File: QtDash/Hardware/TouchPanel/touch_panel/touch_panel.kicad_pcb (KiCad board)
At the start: 2 copper layers, 11 parts, among them U1 74LVC2G14, U2 74LVC2G14, U3 AT42QT1070-S

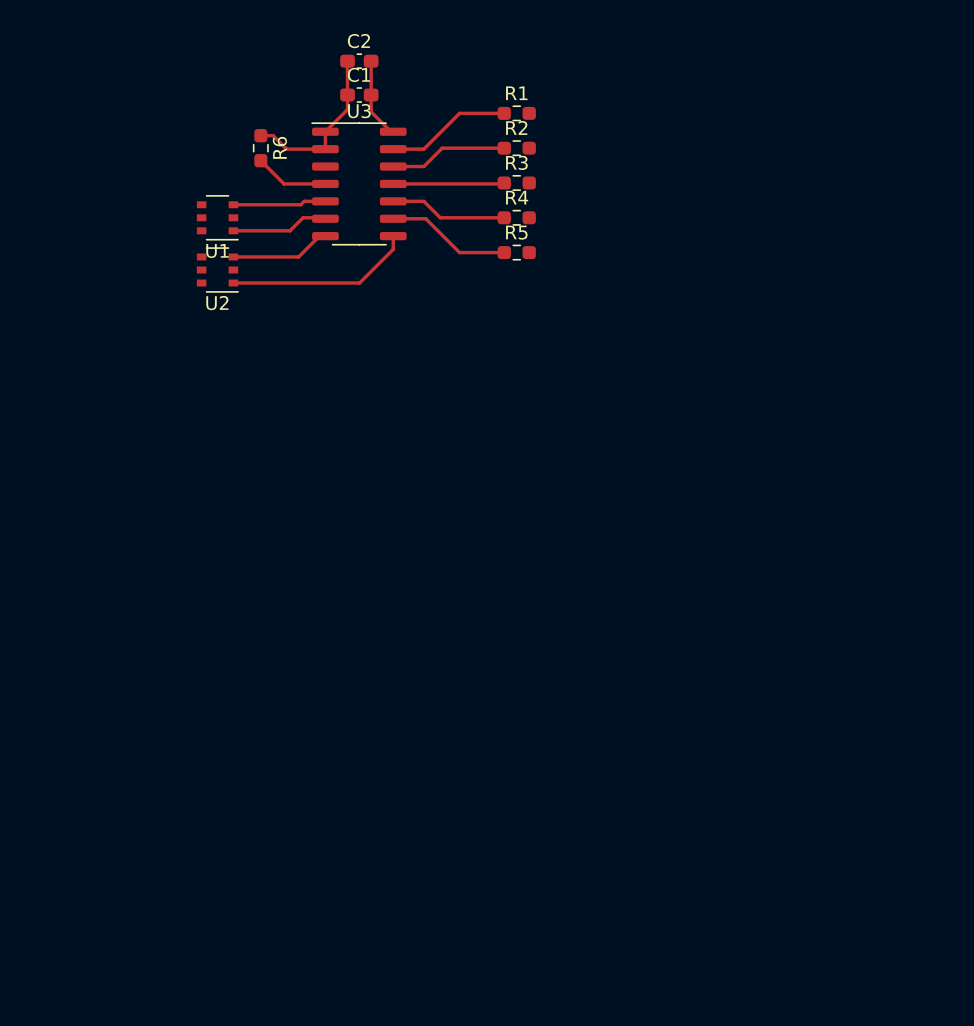
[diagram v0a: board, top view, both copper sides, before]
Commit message: bugfix/hardware-revc-fixes: 	- first draft of layout for control button board 	- added symbol + footprint for capacitive touch button 12.5mm square
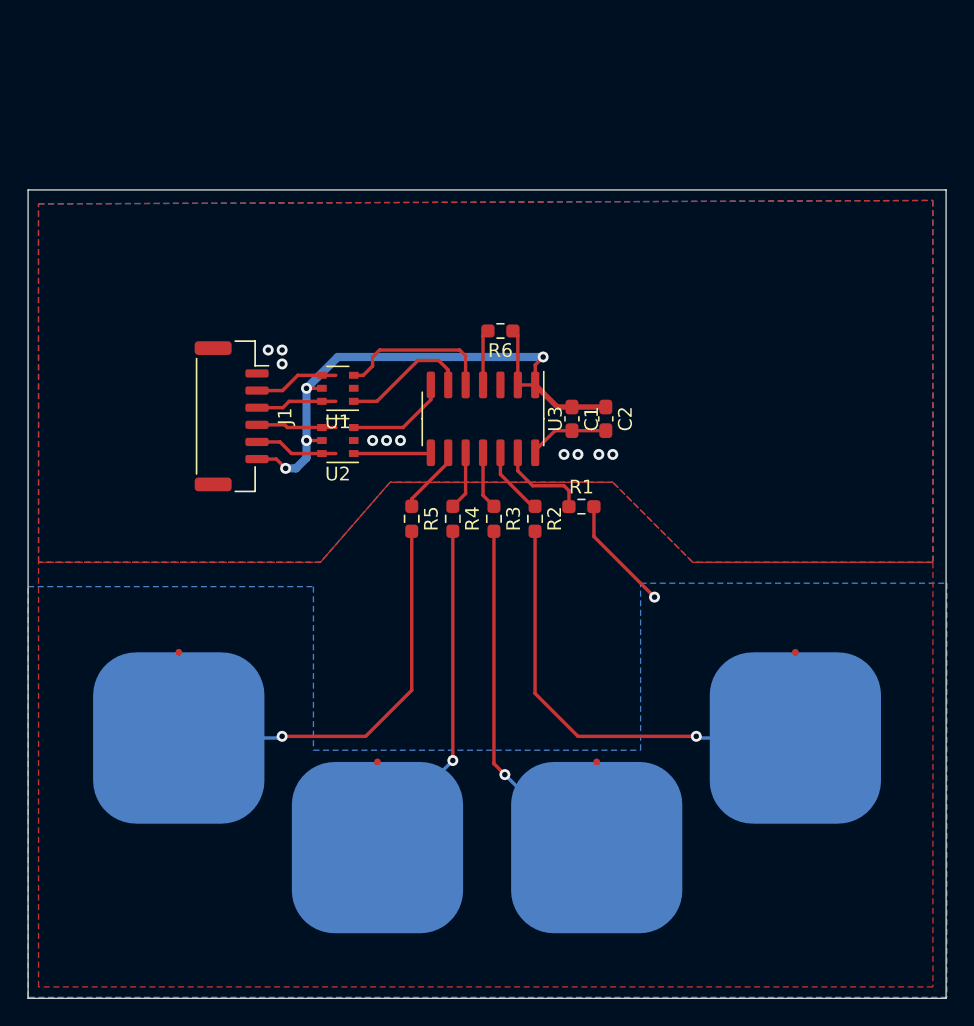
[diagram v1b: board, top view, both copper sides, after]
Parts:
- added J1: Conn_01x06_Male, Connector_JST:JST_GH_SM06B-GHS-TB_1x06-1MP_P1.25mm_Horizontal, F.Cu at (130.7, 92.0)
- added SW1: CapTouch_pad, volvodash:CAPTOUCH_12.5, B.Cu at (171.8, 115.4)
- added SW2: CapTouch_pad, volvodash:CAPTOUCH_12.5, B.Cu at (157.3, 123.4)
- added SW3: CapTouch_pad, volvodash:CAPTOUCH_12.5, B.Cu at (141.3, 123.4)
- added SW4: CapTouch_pad, volvodash:CAPTOUCH_12.5, B.Cu at (126.8, 115.4)
- moved C2 31.7 mm to (158.0, 92.1), turned to -90 degrees
- moved R1 29.1 mm to (156.2, 98.6)
- moved C1 28.3 mm to (155.5, 92.1), turned to -90 degrees
- moved R2 27.1 mm to (152.8, 99.4), turned to -90 degrees
- moved R3 24.6 mm to (149.8, 99.4), turned to -90 degrees
- moved R4 22.5 mm to (146.8, 99.4), turned to -90 degrees
- moved R6 22.0 mm to (150.3, 85.7), turned to 180 degrees
- moved R5 20.9 mm to (143.8, 99.4), turned to -90 degrees
- moved U3 19.4 mm to (149.0, 92.1), turned to -90 degrees
- moved U1 15.2 mm to (138.4, 89.9)
- moved U2 15.2 mm to (138.4, 93.7)
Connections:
- R1 pad 2: unconnected-(R1-Pad2) -> /GUARD_LOOP
- R2 pad 2: unconnected-(R2-Pad2) -> Net-(R2-Pad2)
- R3 pad 2: unconnected-(R3-Pad2) -> Net-(R3-Pad2)
- R4 pad 2: unconnected-(R4-Pad2) -> Net-(R4-Pad2)
- R5 pad 2: unconnected-(R5-Pad2) -> Net-(R5-Pad2)
- U1 pad 4: unconnected-(U1-Pad4) -> /USER_INPUT4
- U1 pad 6: unconnected-(U1-Pad6) -> /USER_INPUT3
- U2 pad 4: unconnected-(U2-Pad4) -> /USER_INPUT2
- U2 pad 6: unconnected-(U2-Pad6) -> /USER_INPUT1
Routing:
- net Net-(R3-Pad2): track 0.00 -> 35.5 mm, vias 0 -> 1
- net Net-(R2-Pad2): track 0.00 -> 34.2 mm, vias 0 -> 1
- net Net-(R4-Pad2): track 0.00 -> 33.9 mm, vias 0 -> 1
- net Net-(R5-Pad2): track 0.00 -> 32.0 mm, vias 0 -> 1
- net VCC: track 12.2 -> 43.2 mm, vias 0 -> 4
- net /GUARD_LOOP: track 0.00 -> 8.44 mm, vias 0 -> 1
- net /OUT1: track 13.6 -> 5.65 mm
- net /USER_INPUT4: track 0.00 -> 6.22 mm
- net /USER_INPUT1: track 0.00 -> 6.11 mm
- net /USER_INPUT3: track 0.00 -> 5.95 mm
- net /USER_INPUT2: track 0.00 -> 5.91 mm
- net /OUT4: track 6.82 -> 11.6 mm
- net /KEY3: track 8.60 -> 4.29 mm
- net /KEY4: track 9.12 -> 5.01 mm
- net /KEY2: track 8.13 -> 4.24 mm
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- added copper zone on B.Cu, net /GUARD_LOOP
- added copper zone on B.Cu, net GND
- added copper zone on F.Cu, net GND
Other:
- board outline added: 67 x 59 mm

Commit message: bugfix/hardware-revc-fixes: 	- finalized touch panel rev A 	- Rev A touch panel board sent to fab 	- added stl files for small guage slot cover (whole and cutout for touch panel board)
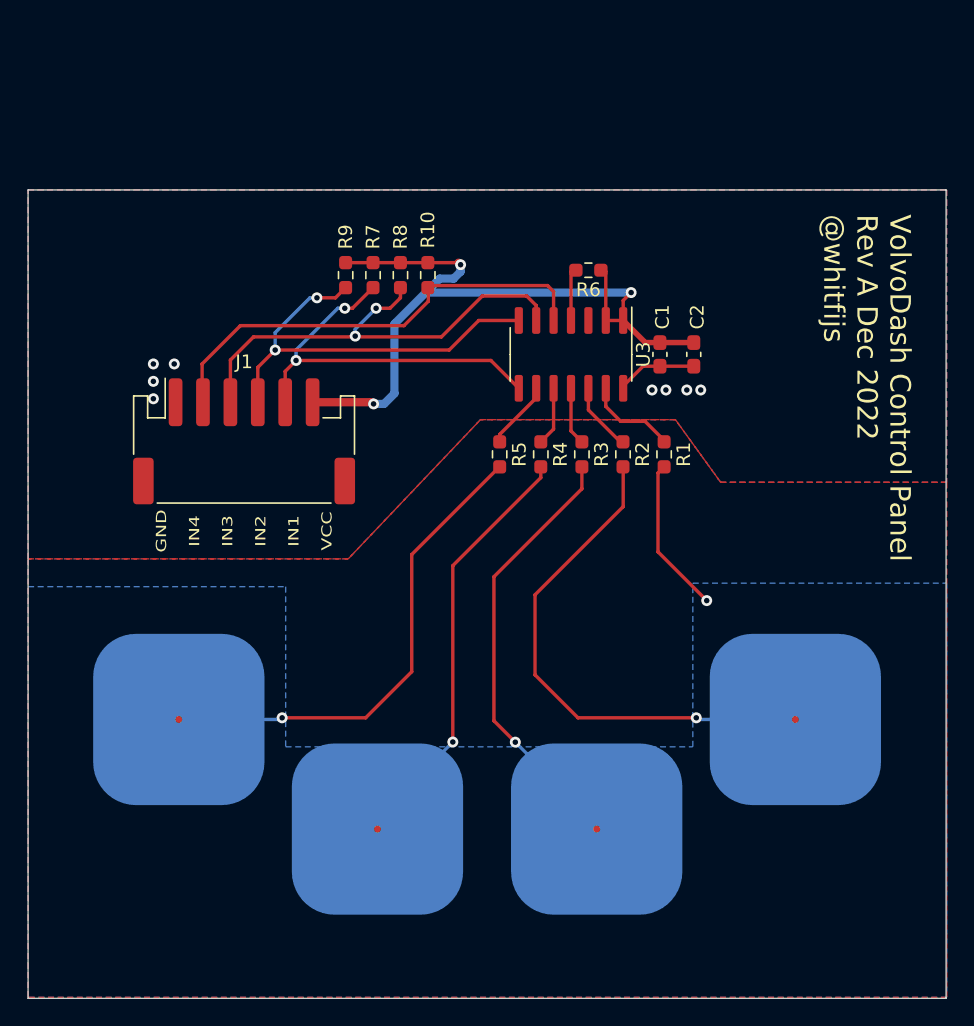
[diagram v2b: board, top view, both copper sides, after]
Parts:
- removed U1, U2: 74LVC2G14, Package_SO:TSOP-6_1.65x3.05mm_P0.95mm
- added R10: 10k, Resistor_SMD:R_0603_1608Metric_Pad0.98x0.95mm_HandSolder, F.Cu at (145.0, 81.7)
- added R7: 10k, Resistor_SMD:R_0603_1608Metric_Pad0.98x0.95mm_HandSolder, F.Cu at (141.0, 81.7)
- added R8: 10k, Resistor_SMD:R_0603_1608Metric_Pad0.98x0.95mm_HandSolder, F.Cu at (143.0, 81.7)
- added R9: 10k, Resistor_SMD:R_0603_1608Metric_Pad0.98x0.95mm_HandSolder, F.Cu at (139.0, 81.7)
- J1: footprint Connector_JST:JST_GH_SM06B-GHS-TB_1x06-1MP_P1.25mm_Horizontal -> Connector_JST:JST_PH_S6B-PH-SM4-TB_1x06-1MP_P2.00mm_Horizontal
- moved U3 7.96 mm to (155.4, 87.4)
- moved R2 7.96 mm to (159.2, 94.7)
- moved R3 7.96 mm to (156.2, 94.7)
- moved R4 7.96 mm to (153.2, 94.7)
- moved R5 7.96 mm to (150.2, 94.7)
- moved C1 7.96 mm to (161.9, 87.4)
- moved C2 7.96 mm to (164.4, 87.4)
- moved R6 7.80 mm to (156.7, 81.3)
- moved R1 7.14 mm to (162.2, 94.7), turned to -90 degrees
- moved J1 2.04 mm to (131.6, 93.8), turned to 0 degrees
- moved SW1 1.35 mm to (171.8, 114.1)
- moved SW2 1.35 mm to (157.3, 122.1)
- moved SW3 1.35 mm to (141.3, 122.1)
- moved SW4 1.35 mm to (126.8, 114.1)
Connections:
- J1 pad 2: /USER_INPUT4 -> /OUT4
- J1 pad 3: /USER_INPUT3 -> /OUT3
- J1 pad 4: /USER_INPUT2 -> /OUT2
- J1 pad 5: /USER_INPUT1 -> /OUT1
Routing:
- net /OUT3: track 9.51 -> 34.2 mm, vias 0 -> 2
- net /OUT2: track 7.55 -> 30.8 mm, vias 0 -> 2
- net /OUT1: track 5.65 -> 28.7 mm, vias 0 -> 2
- net /OUT4: track 11.6 -> 33.8 mm
- net VCC: track 43.2 -> 55.2 mm, vias 4 -> 3
- net /USER_INPUT4: track 6.22 -> 0.00 mm
- net /USER_INPUT1: track 6.11 -> 0.00 mm
- net Net-(R2-Pad2): track 34.2 -> 40.2 mm
- net Net-(R5-Pad2): track 32.0 -> 38.0 mm
- net /USER_INPUT3: track 5.95 -> 0.00 mm
- net /USER_INPUT2: track 5.91 -> 0.00 mm
- net Net-(R3-Pad2): track 35.5 -> 32.2 mm
- net /GUARD_LOOP: track 8.44 -> 11.4 mm
- net Net-(R4-Pad2): track 33.9 -> 31.4 mm
- net GND: vias 10 -> 8
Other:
- board text added: "GND IN4 IN3 IN2 IN1 VCC"
- board text added: "VolvoDash Control Panel Rev A Dec 2022 @whitfijs"
